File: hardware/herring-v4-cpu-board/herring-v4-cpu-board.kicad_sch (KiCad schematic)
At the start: 17 parts, among them J1 Conn_02x20_Odd_Even, J2 Conn_02x10_Odd_Even, U1 W65C02, U2 ATF16V8B, U3 AT28C64B, U4 AS6C62256, X1 CXO_DIP8

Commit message: CPU board schematic mostly done, started routing
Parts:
- removed C1: C, Capacitor_THT:C_Disc_D4.3mm_W1.9mm_P5.00mm, symbol Device:C
- removed U2: ATF16V8B, Package_DIP:DIP-20_W7.62mm, symbol herring:ATF16V8B
- removed U3: AT28C64B, Package_DIP:DIP-28_W15.24mm, symbol herring:AT28C64B
- removed U4: AS6C62256, Package_DIP:DIP-28_W15.24mm, symbol herring:AS6C62256
- added C1: C_Polarized, Capacitor_THT:CP_Radial_D10.0mm_P3.80mm, symbol Device:C_Polarized
- added C10, C11, C12, C6, C7, C8, C9: C, Capacitor_THT:C_Disc_D5.0mm_W2.5mm_P5.00mm, symbol Device:C
- added R6: R, Resistor_THT:R_Axial_DIN0207_L6.3mm_D2.5mm_P7.62mm_Horizontal, symbol Device:R
- added U10: AS6C4008-55PCN, Package_DIP:DIP-32_W15.24mm, symbol Memory_RAM:AS6C4008-55PCN
- added U11, U3: ATF22V10C, Package_DIP:DIP-24_W7.62mm, symbol mackerel-68k-symbols:ATF22V10C
- added U2, U4, U5, U6: 74HC245, Package_DIP:DIP-20_W7.62mm, symbol 74xx:74HC245
- added U8: W65C22, Package_DIP:DIP-40_W15.24mm, symbol herring:W65C22
- added U9: SST39SF040, Package_DIP:DIP-32_W15.24mm, symbol Memory_Flash:SST39SF040
- C2, C3, C4, C5: footprint Capacitor_THT:C_Disc_D4.3mm_W1.9mm_P5.00mm -> Capacitor_THT:C_Disc_D5.0mm_W2.5mm_P5.00mm
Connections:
- net /WR is gone; now on net /NMI: J1.34 (Pin_34)
- net +5V: now also C1.1, C10.1, C11.1, C12.1, C6.1, C7.1, C8.1, C9.1, R6.1, U10.32 (VCC), U11.24 (vcc), U2.20 (VCC), U3.24 (vcc), U4.20 (VCC), U5.20 (VCC), U6.1 (A->B), U6.20 (VCC), U8.20 (VCC), U8.24 (CS1), U9.31 (PGM), U9.32 (VCC); no longer U1.38 (~{SO})
- net A0: now also U2.9 (A7); no longer U1.9 (A0)
- net A1: now also U2.8 (A6); no longer U1.10 (A1)
- net A10: now also U4.7 (A5); no longer U1.19 (A10)
- net A11: now also U4.6 (A4); no longer U1.20 (A11)
- net A12: now also U4.5 (A3); no longer U1.22 (A12)
- net A13: now also U4.4 (A2); no longer U1.23 (A13)
- net A14: now also U4.3 (A1); no longer U1.24 (A14)
- net A15: now also U4.2 (A0); no longer U1.25 (A15)
- net A2: now also U2.7 (A5); no longer U1.11 (A2)
- net A3: now also U2.6 (A4); no longer U1.12 (A3)
- net A4: now also U2.5 (A3); no longer U1.13 (A4)
- net A5: now also U2.4 (A2); no longer U1.14 (A5)
- net A6: now also U2.3 (A1); no longer U1.15 (A6)
- net A7: now also U2.2 (A0); no longer U1.16 (A7)
- net A8: now also U4.9 (A7); no longer U1.17 (A8)
- net A9: now also U4.8 (A6); no longer U1.18 (A9)
- net BE: now also J1.35 (Pin_35), U3.1 (CLK/IN0); no longer J2.5 (Pin_5)
- net CLK: now also U6.18 (B0); no longer U1.37 (PHI2), X1.5 (OUT)
- net D0: now also U5.9 (A7); no longer U1.33 (D0)
- net D1: now also U5.8 (A6); no longer U1.32 (D1)
- net D2: now also U5.7 (A5); no longer U1.31 (D2)
- net D3: now also U5.6 (A4); no longer U1.30 (D3)
- net D4: now also U5.5 (A3); no longer U1.29 (D4)
- net D5: now also U5.4 (A2); no longer U1.28 (D5)
- net D6: now also U5.3 (A1); no longer U1.27 (D6)
- net D7: now also U5.2 (A0); no longer U1.26 (D7)
- net GND: now also C1.2, C10.2, C11.2, C12.2, C6.2, C7.2, C8.2, C9.2, U10.16 (VSS), U10.24 (OE#), U11.12 (GND), U2.1 (A->B), U2.10 (GND), U3.12 (GND), U3.13 (IN11), U4.1 (A->B), U4.10 (GND), U5.10 (GND), U6.10 (GND), U6.4 (A2), U6.5 (A3), U6.6 (A4), U6.7 (A5), U6.8 (A6), U6.9 (A7), U8.1 (GND), U9.1 (A18), U9.16 (GND), U9.2 (A16), U9.24 (OE), U9.28 (A13), U9.29 (A14), U9.3 (A15), U9.30 (A17)
- net RDY: now also J1.36 (Pin_36), R6.2; no longer J2.4 (Pin_4), R5.2
- net /IRQ: now also U11.14 (IO0); no longer J1.35 (Pin_35)
- net /NMI: no longer J1.36 (Pin_36)
- net /RES: now also U8.34 (/RES)
- net /RW: now also U6.17 (B1); no longer U1.34 (~{RW})
- net SPI_CLK: now reaches J2.10 (Pin_10)
- net SPI_CLK: now also U8.10 (PB0)
- net SPI_DI: now reaches J2.11 (Pin_11)
- net SPI_DI: now also U8.11 (PB1)
- net SPI_DO: now reaches J2.12 (Pin_12)
- net SPI_DO: now also U8.12 (PB2)
- net SPI_CS0: now reaches J2.13 (Pin_13)
- net SPI_CS0: now also U8.13 (PB3)
- net SPI_CS1: now reaches J2.14 (Pin_14)
- net SPI_CS1: now also U8.14 (PB4)
- net SPI_CS2: now reaches J2.15 (Pin_15)
- net SPI_CS2: now also U8.15 (PB5)
- net SPI_CS3: now reaches J2.16 (Pin_16)
- net SPI_CS3: now also U8.16 (PB6)
- net SPI_INT0: now reaches J2.17 (Pin_17)
- net SPI_INT0: now also U8.18 (CB1)
- net SPI_INT1: now reaches J2.18 (Pin_18)
- net SPI_INT1: now also U8.19 (CB2)
- net /CS5: now reaches J2.8 (Pin_8)
- net /CS5: now also U3.18 (IO4)
- net /CS6: now reaches J2.9 (Pin_9)
- net /CS6: now also U3.17 (IO3)
- net SYNC: no longer names the net of U1.7 (SYNC)
- net SYNC: no longer J2.6 (Pin_6)
- net /CS_IO renamed /IRQEXP
- net /IRQEXP: now also U11.11 (IN10)
- net /ML: no longer names the net of U1.5 (~{ML})
- net /ML: no longer J2.3 (Pin_3)
- net /VP: no longer names the net of U1.1 (~{VP})
- net /VP: no longer J2.7 (Pin_7)
- new net: R5.2, U1.38 (~{SO})
- new net A0CPU: U1.9 (A0), U10.12 (A0), U2.11 (B7), U8.38 (RS0), U9.12 (A0)
- new net A10CPU: U1.19 (A10), U10.23 (A10), U3.6 (IN5), U4.13 (B5), U9.23 (A10)
- new net A11CPU: U1.20 (A11), U10.25 (A11), U3.7 (IN6), U4.14 (B4), U9.25 (A11)
- new net A12CPU: U1.22 (A12), U10.4 (A12), U3.8 (IN7), U4.15 (B3), U9.4 (A12)
- new net A13CPU: U1.23 (A13), U10.28 (A13), U11.2 (IN1), U3.9 (IN8), U4.16 (B2)
- new net A14CPU: U1.24 (A14), U11.3 (IN2), U3.10 (IN9), U4.17 (B1)
- new net A14_RAM: U10.3 (A14), U11.23 (IO9)
- new net A14_VIA: U11.5 (IN4), U8.2 (PA0)
- new net A15CPU: U1.25 (A15), U11.4 (IN3/PD), U3.11 (IN10), U4.18 (B0)
- new net A15_RAM: U10.31 (A15), U11.22 (IO8)
- new net A15_VIA: U11.6 (IN5), U8.3 (PA1)
- new net A16_RAM: U10.2 (A16), U11.21 (IO7)
- new net A16_VIA: U11.7 (IN6), U8.4 (PA2)
- new net A17_RAM: U10.30 (A17), U11.20 (IO6)
- new net A17_VIA: U11.8 (IN7), U8.5 (PA3)
- new net A18_RAM: U10.1 (A18), U11.19 (IO5)
- new net A18_VIA: U11.9 (IN8), U8.6 (PA4)
- new net A1CPU: U1.10 (A1), U10.11 (A1), U2.12 (B6), U8.37 (RS1), U9.11 (A1)
- new net A2CPU: U1.11 (A2), U10.10 (A2), U2.13 (B5), U8.36 (RS2), U9.10 (A2)
- new net A3CPU: U1.12 (A3), U10.9 (A3), U2.14 (B4), U8.35 (RS3), U9.9 (A3)
- new net A4CPU: U1.13 (A4), U10.8 (A4), U2.15 (B3), U9.8 (A4)
- new net A5CPU: U1.14 (A5), U10.7 (A5), U2.16 (B2), U9.7 (A5)
- new net A6CPU: U1.15 (A6), U10.6 (A6), U2.17 (B1), U3.2 (IN1), U9.6 (A6)
- new net A7CPU: U1.16 (A7), U10.5 (A7), U2.18 (B0), U3.3 (IN2), U9.5 (A7)
- new net A8CPU: U1.17 (A8), U10.27 (A8), U3.4 (IN3/PD), U4.11 (B7), U9.27 (A8)
- new net A9CPU: U1.18 (A9), U10.26 (A9), U3.5 (IN4), U4.12 (B6), U9.26 (A9)
- new net CLKCPU: U1.37 (PHI2), U11.1 (CLK/IN0), U6.2 (A0), U8.25 (PHI2), X1.5 (OUT)
- new net D0CPU: U1.33 (D0), U10.13 (DQ0), U5.11 (B7), U8.33 (D0), U9.13 (D0)
- new net D1CPU: U1.32 (D1), U10.14 (DQ1), U5.12 (B6), U8.32 (D1), U9.14 (D1)
- new net D2CPU: U1.31 (D2), U10.15 (DQ2), U5.13 (B5), U8.31 (D2), U9.15 (D2)
- new net D3CPU: U1.30 (D3), U10.17 (DQ3), U5.14 (B4), U8.30 (D3), U9.17 (D3)
- new net D4CPU: U1.29 (D4), U10.18 (DQ4), U5.15 (B3), U8.29 (D4), U9.18 (D4)
- new net D5CPU: U1.28 (D5), U10.19 (DQ5), U5.16 (B2), U8.28 (D5), U9.19 (D5)
- new net D6CPU: U1.27 (D6), U10.20 (DQ6), U5.17 (B1), U8.27 (D6), U9.20 (D6)
- new net D7CPU: U1.26 (D7), U10.21 (DQ7), U5.18 (B0), U8.26 (D7), U9.21 (D7)
- new net /BUFFERS: U2.19 (CE), U3.14 (IO0), U4.19 (CE), U5.19 (CE), U6.19 (CE)
- new net /CS0: J2.3 (Pin_3), U3.23 (IO9)
- new net /CS1: J2.4 (Pin_4), U3.22 (IO8)
- new net /CS2: J2.5 (Pin_5), U3.21 (IO7)
- new net /CS3: J2.6 (Pin_6), U3.20 (IO6)
- new net /CS4: J2.7 (Pin_7), U3.19 (IO5)
- new net /CSVIA: U3.16 (IO2), U8.23 (/CS2)
- new net /CS_RAM: U10.22 (CE#), U11.18 (IO4)
- new net /CS_ROM: U11.17 (IO3), U9.22 (CE)
- new net /IRQVIA: U11.10 (IN9), U8.21 (/IRQ)
- new net /RAM_WR: U10.29 (WE#), U11.16 (IO2)
- new net /RWCPU: U1.34 (~{RW}), U11.13 (IN11), U5.1 (A->B), U6.3 (A1), U8.22 (/RW)
- no-connect marks 18 -> 20
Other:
- note added: "512KB Flash ROM (8KB usable)"
- note added: "512KB SRAM"
- note added: "60 Pin Expansion Header"
- note added: "65C02 CPU"
- note added: "65C22 VIA"
- note added: "Control Signals Buffer"
- note added: "Data Bus Buffer"
- note added: "I/O Decoder"
- note added: "Lower Address Bus Buffer"
- note added: "Memory Decoder"
- note added: "TODO: power and user LEDs"
- note added: "TODO: pullup on IRQ exp"
- note added: "Upper Address Bus Buffer"
- moved on the sheet: J1, J2, R1, R2, R3, R4, R5, U1, X1

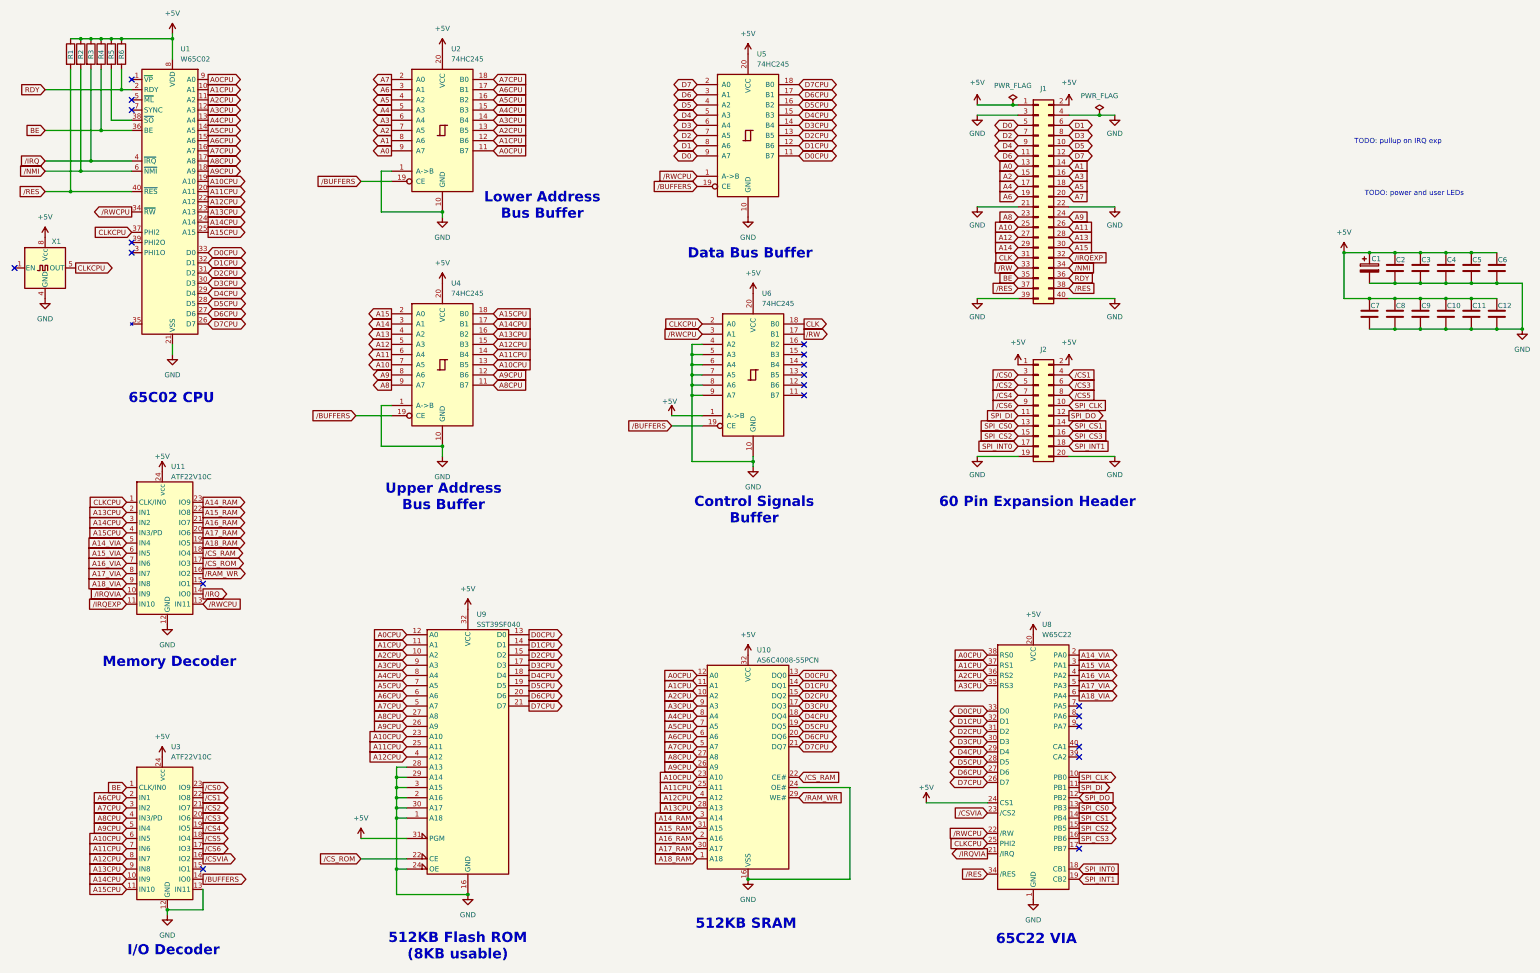
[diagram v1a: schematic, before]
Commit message: Routed buffers and expansion header
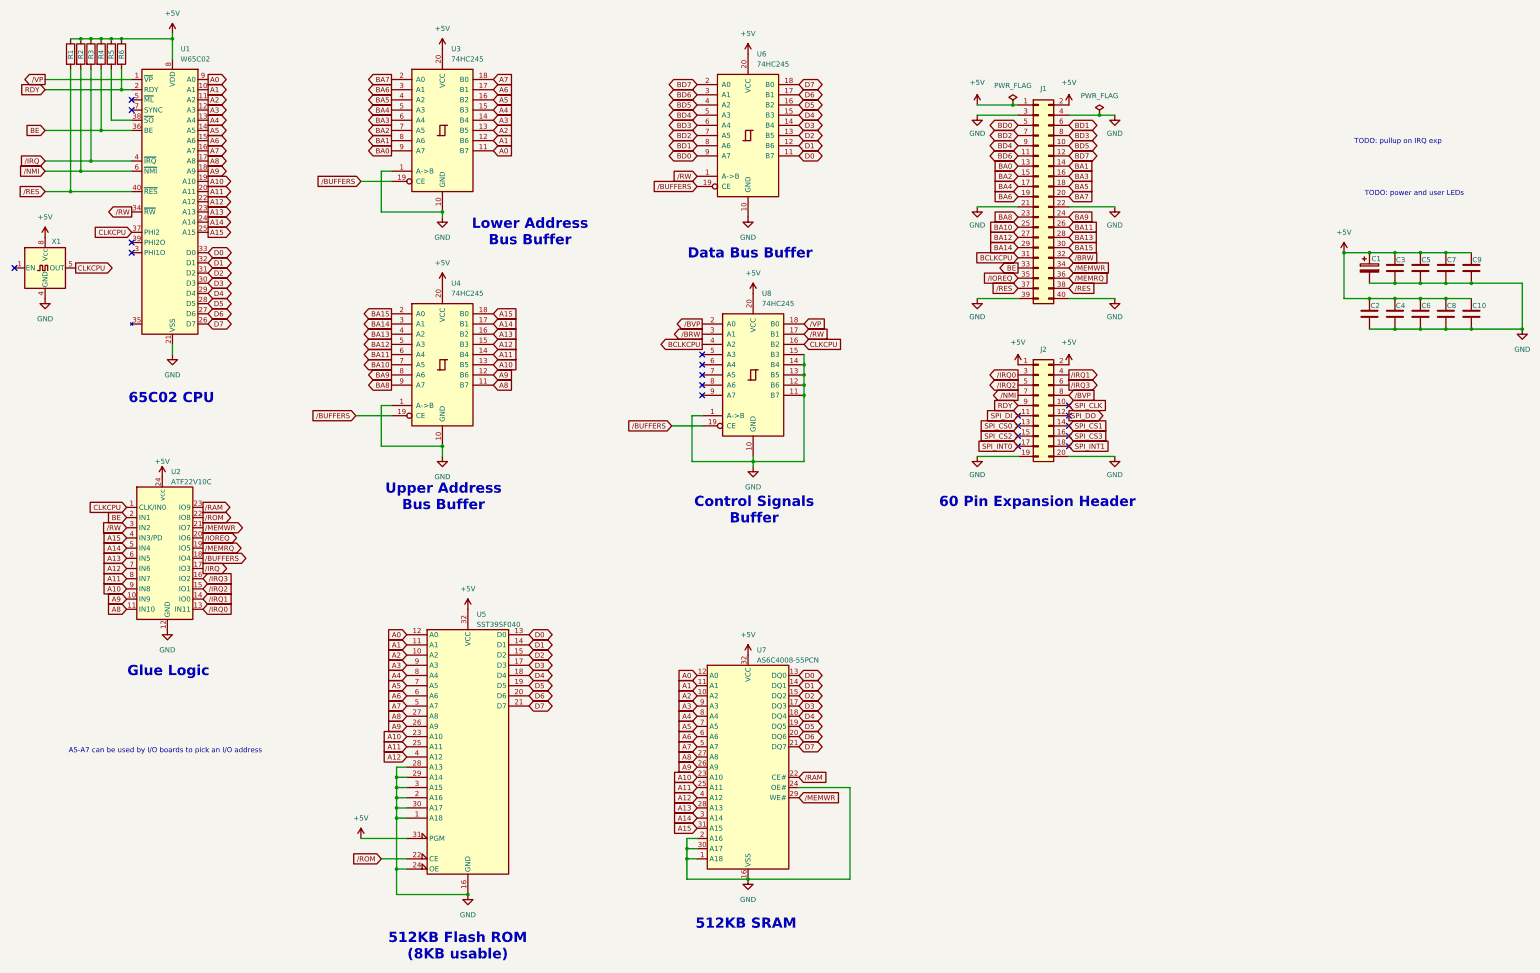
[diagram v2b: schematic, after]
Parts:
- removed C12, C6: C, Capacitor_THT:C_Disc_D5.0mm_W2.5mm_P5.00mm, symbol Device:C
- removed U11, U3: ATF22V10C, Package_DIP:DIP-24_W7.62mm, symbol mackerel-68k-symbols:ATF22V10C
- removed U8: W65C22, Package_DIP:DIP-40_W15.24mm, symbol herring:W65C22
- added U2: ATF22V10C, Package_DIP:DIP-24_W7.62mm, symbol mackerel-68k-symbols:ATF22V10C
- renumbered C11 to C10, C7 to C2, C2 to C3, C8 to C4, C3 to C5, C9 to C6, C4 to C7, C10 to C8, C5 to C9, U2 to U3, U9 to U5, U5 to U6, U10 to U7, U6 to U8
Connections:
- net A0CPU is gone; now on net A0: U1.9 (A0), U3.11 (B7), U5.12 (A0), U7.12 (A0)
- net A10CPU is gone; now on net A10: U1.19 (A10), U4.13 (B5), U5.23 (A10), U7.23 (A10)
- net A11CPU is gone; now on net A11: U1.20 (A11), U4.14 (B4), U5.25 (A11), U7.25 (A11)
- net A12CPU is gone; now on net A12: U1.22 (A12), U4.15 (B3), U5.4 (A12), U7.4 (A12)
- net A13CPU is gone; now on net A13: U1.23 (A13), U4.16 (B2), U7.28 (A13)
- net A14CPU is gone; now on net A14: U1.24 (A14), U4.17 (B1)
- net A14_RAM is gone; now on net A14: U7.3 (A14)
- net A15CPU is gone; now on net A15: U1.25 (A15), U4.18 (B0)
- net A15_RAM is gone; now on net A15: U7.31 (A15)
- net A16_RAM is gone; now on net GND: U7.2 (A16)
- net A17_RAM is gone; now on net GND: U7.30 (A17)
- net A18_RAM is gone; now on net GND: U7.1 (A18)
- net A1CPU is gone; now on net A1: U1.10 (A1), U3.12 (B6), U5.11 (A1), U7.11 (A1)
- net A2CPU is gone; now on net A2: U1.11 (A2), U3.13 (B5), U5.10 (A2), U7.10 (A2)
- net A3CPU is gone; now on net A3: U1.12 (A3), U3.14 (B4), U5.9 (A3), U7.9 (A3)
- net A4CPU is gone; now on net A4: U1.13 (A4), U3.15 (B3), U5.8 (A4), U7.8 (A4)
- net A5CPU is gone; now on net A5: U1.14 (A5), U3.16 (B2), U5.7 (A5), U7.7 (A5)
- net A6CPU is gone; now on net A6: U1.15 (A6), U3.17 (B1), U5.6 (A6), U7.6 (A6)
- net A7CPU is gone; now on net A7: U1.16 (A7), U3.18 (B0), U5.5 (A7), U7.5 (A7)
- net A8CPU is gone; now on net A8: U1.17 (A8), U4.11 (B7), U5.27 (A8), U7.27 (A8)
- net A9CPU is gone; now on net A9: U1.18 (A9), U4.12 (B6), U5.26 (A9), U7.26 (A9)
- net D0CPU is gone; now on net D0: U1.33 (D0), U5.13 (D0), U6.11 (B7), U7.13 (DQ0)
- net D1CPU is gone; now on net D1: U1.32 (D1), U5.14 (D1), U6.12 (B6), U7.14 (DQ1)
- net D2CPU is gone; now on net D2: U1.31 (D2), U5.15 (D2), U6.13 (B5), U7.15 (DQ2)
- net D3CPU is gone; now on net D3: U1.30 (D3), U5.17 (D3), U6.14 (B4), U7.17 (DQ3)
- net D4CPU is gone; now on net D4: U1.29 (D4), U5.18 (D4), U6.15 (B3), U7.18 (DQ4)
- net D5CPU is gone; now on net D5: U1.28 (D5), U5.19 (D5), U6.16 (B2), U7.19 (DQ5)
- net D6CPU is gone; now on net D6: U1.27 (D6), U5.20 (D6), U6.17 (B1), U7.20 (DQ6)
- net D7CPU is gone; now on net D7: U1.26 (D7), U5.21 (D7), U6.18 (B0), U7.21 (DQ7)
- net /CS4 is gone; now on net /NMI: J2.7 (Pin_7)
- net /CS6 is gone; now on net RDY: J2.9 (Pin_9)
- net +5V: now also U2.24 (vcc); no longer U8.1 (A->B)
- net A0: no longer J1.13 (Pin_13), U3.9 (A7)
- net A1: no longer J1.14 (Pin_14), U3.8 (A6)
- net A10: now also U2.9 (IN8); no longer J1.25 (Pin_25), U4.7 (A5)
- net A11: now also U2.8 (IN7); no longer J1.26 (Pin_26), U4.6 (A4)
- net A12: now also U2.7 (IN6); no longer J1.27 (Pin_27), U4.5 (A3)
- net A13: now also U2.6 (IN5); no longer J1.28 (Pin_28), U4.4 (A2)
- net A14: now also U2.5 (IN4); no longer J1.29 (Pin_29), U4.3 (A1)
- net A15: now also U2.4 (IN3/PD); no longer J1.30 (Pin_30), U4.2 (A0)
- net A2: no longer J1.15 (Pin_15), U3.7 (A5)
- net A3: no longer J1.16 (Pin_16), U3.6 (A4)
- net A4: no longer J1.17 (Pin_17), U3.5 (A3)
- net A5: no longer J1.18 (Pin_18), U3.4 (A2)
- net A6: no longer J1.19 (Pin_19), U3.3 (A1)
- net A7: no longer J1.20 (Pin_20), U3.2 (A0)
- net A8: now also U2.11 (IN10); no longer J1.23 (Pin_23), U4.9 (A7)
- net A9: now also U2.10 (IN9); no longer J1.24 (Pin_24), U4.8 (A6)
- net BE: now also J1.33 (Pin_33), U2.2 (IN1); no longer J1.35 (Pin_35)
- net CLKCPU: now also U8.16 (B2), U2.1 (CLK/IN0); no longer U8.2 (A0)
- net D0: no longer J1.5 (Pin_5), U6.9 (A7)
- net D1: no longer J1.6 (Pin_6), U6.8 (A6)
- net D2: no longer J1.7 (Pin_7), U6.7 (A5)
- net D3: no longer J1.8 (Pin_8), U6.6 (A4)
- net D4: no longer J1.9 (Pin_9), U6.5 (A3)
- net D5: no longer J1.10 (Pin_10), U6.4 (A2)
- net D6: no longer J1.11 (Pin_11), U6.3 (A1)
- net D7: no longer J1.12 (Pin_12), U6.2 (A0)
- net GND: now also U8.1 (A->B), U8.11 (B7), U8.12 (B6), U8.13 (B5), U8.14 (B4), U8.15 (B3), U2.12 (GND); no longer U8.4 (A2), U8.5 (A3), U8.6 (A4), U8.7 (A5), U8.8 (A6), U8.9 (A7)
- net RDY: no longer J1.36 (Pin_36)
- net /BUFFERS: now also U2.18 (IO4)
- net /IRQ: now also U2.17 (IO3)
- net /NMI: no longer J1.34 (Pin_34)
- net /RW: now also U1.34 (~{RW}), U6.1 (A->B), U2.3 (IN2); no longer J1.33 (Pin_33)
- net /VP: now reaches U1.1 (~{VP})
- net /VP: now also U8.18 (B0)
- net CLK renamed BCLKCPU
- net BCLKCPU: now also U8.4 (A2); no longer U8.18 (B0)
- net /CS0 renamed /IRQ0
- net /IRQ0: now also U2.13 (IN11)
- net /CS1 renamed /IRQ1
- net /IRQ1: now also U2.14 (IO0)
- net /CS2 renamed /IRQ2
- net /IRQ2: now also U2.15 (IO1)
- net /CS3 renamed /IRQ3
- net /IRQ3: now also U2.16 (IO2)
- net /CS5 renamed /BVP
- net /BVP: now also U8.2 (A0)
- net /CS_RAM renamed /RAM
- net /RAM: now also U2.23 (IO9)
- net /CS_ROM renamed /ROM
- net /ROM: now also U2.22 (IO8)
- net /IRQEXP renamed /BRW
- net /BRW: now also U8.3 (A1)
- net /RAM_WR renamed /MEMWR
- net /MEMWR: now also J1.34 (Pin_34), U2.21 (IO7)
- removed net /RWCPU: U1.34 (~{RW}), U6.1 (A->B), U8.3 (A1)
- new net BA0: J1.13 (Pin_13), U3.9 (A7)
- new net BA1: J1.14 (Pin_14), U3.8 (A6)
- new net BA10: J1.25 (Pin_25), U4.7 (A5)
- new net BA11: J1.26 (Pin_26), U4.6 (A4)
- new net BA12: J1.27 (Pin_27), U4.5 (A3)
- new net BA13: J1.28 (Pin_28), U4.4 (A2)
- new net BA14: J1.29 (Pin_29), U4.3 (A1)
- new net BA15: J1.30 (Pin_30), U4.2 (A0)
- new net BA2: J1.15 (Pin_15), U3.7 (A5)
- new net BA3: J1.16 (Pin_16), U3.6 (A4)
- new net BA4: J1.17 (Pin_17), U3.5 (A3)
- new net BA5: J1.18 (Pin_18), U3.4 (A2)
- new net BA6: J1.19 (Pin_19), U3.3 (A1)
- new net BA7: J1.20 (Pin_20), U3.2 (A0)
- new net BA8: J1.23 (Pin_23), U4.9 (A7)
- new net BA9: J1.24 (Pin_24), U4.8 (A6)
- new net BD0: J1.5 (Pin_5), U6.9 (A7)
- new net BD1: J1.6 (Pin_6), U6.8 (A6)
- new net BD2: J1.7 (Pin_7), U6.7 (A5)
- new net BD3: J1.8 (Pin_8), U6.6 (A4)
- new net BD4: J1.9 (Pin_9), U6.5 (A3)
- new net BD5: J1.10 (Pin_10), U6.4 (A2)
- new net BD6: J1.11 (Pin_11), U6.3 (A1)
- new net BD7: J1.12 (Pin_12), U6.2 (A0)
- new net /IOREQ: J1.35 (Pin_35), U2.20 (IO6)
- new net /MEMRQ: J1.36 (Pin_36), U2.19 (IO5)
- no-connect marks 20 -> 19
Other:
- note added: "A5-A7 can be used by I/O boards to pick an I/O address"
- note added: "Glue Logic"
- note removed: "65C22 VIA"
- note removed: "I/O Decoder"
- note removed: "Memory Decoder"

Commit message: v4 CPU board fully routed, needs cleanup
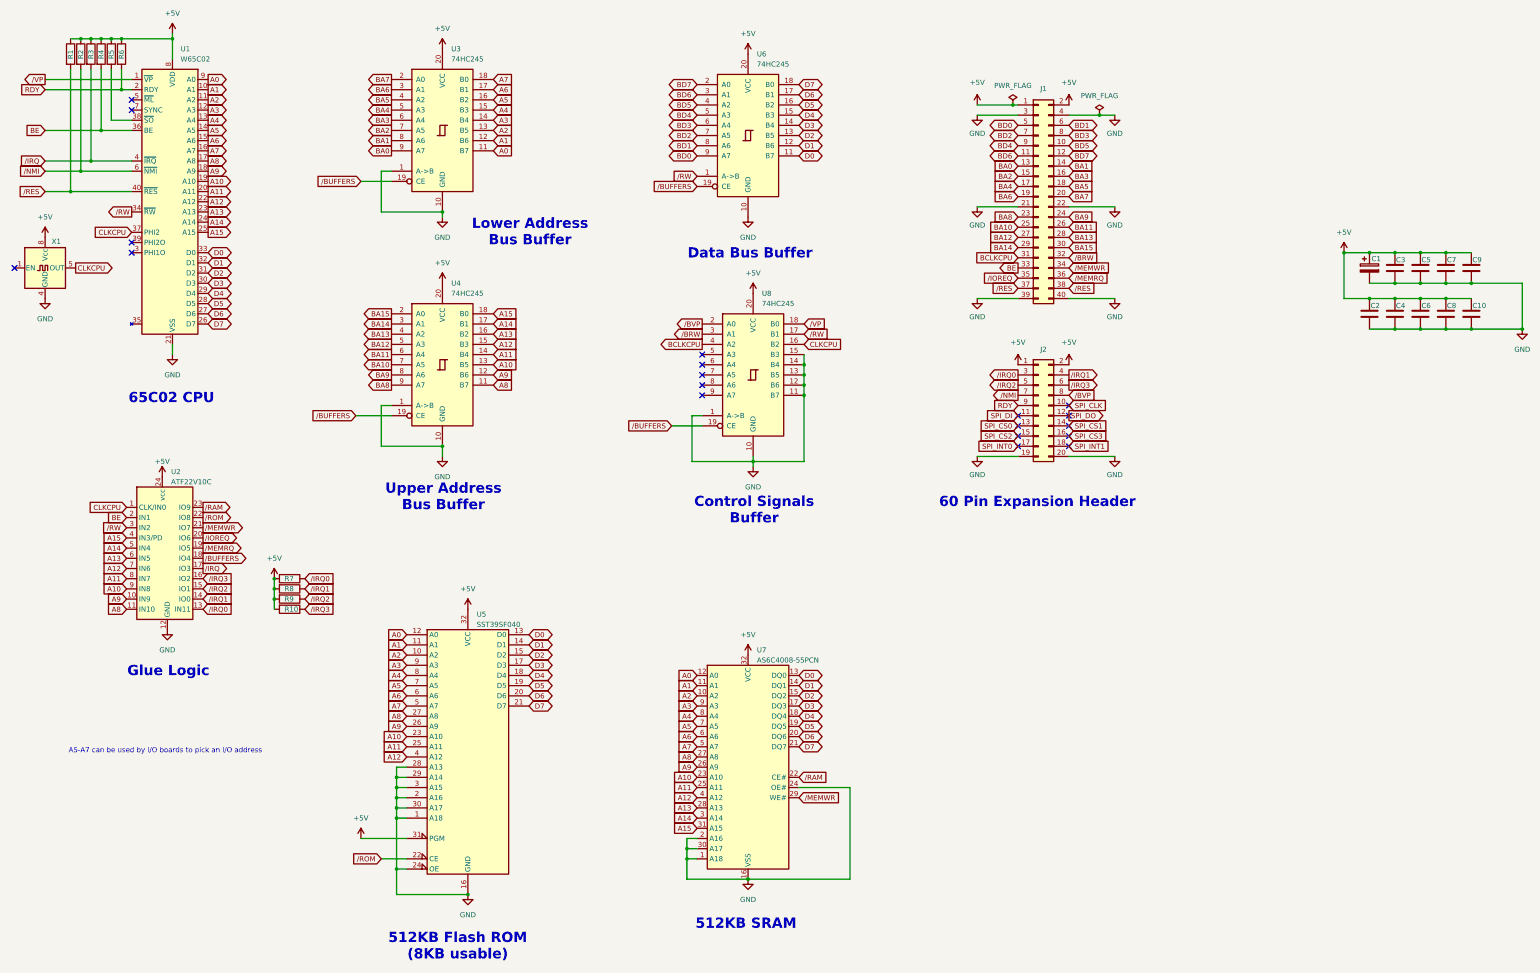
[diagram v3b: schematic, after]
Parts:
- added R10, R7, R8, R9: R, Resistor_THT:R_Axial_DIN0207_L6.3mm_D2.5mm_P7.62mm_Horizontal, symbol Device:R
- U5: footprint Package_DIP:DIP-32_W15.24mm -> Socket:DIP_Socket-32_W11.9_W12.7_W15.24_W17.78_W18.5_3M_232-1285-00-0602J
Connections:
- net +5V: now also R10.2, R7.2, R8.2, R9.2
- net /IRQ0: now also R7.1
- net /IRQ1: now also R8.1
- net /IRQ2: now also R9.1
- net /IRQ3: now also R10.1
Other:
- note removed: "TODO: power and user LEDs"
- note removed: "TODO: pullup on IRQ exp"
